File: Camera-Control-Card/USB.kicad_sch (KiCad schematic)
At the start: 15 parts, among them J9 USB_C_Receptacle_USB2.0_16P, U6 TPD2EUSB30, U7 CP2102N-Axx-xQFN20

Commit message: Camera Control Card layout
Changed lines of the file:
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@@
+	)
+	(junction
+		(at 152.4 115.57)
+		(diameter 0)
+		(color 0 0 0 0)
 	)
 	(junction
@@
 	)
 	(junction
+		(at 226.06 50.8)
+		(diameter 0)
+		(color 0 0 0 0)
+	)
+	(junction
 		(at 146.05 115.57)
 		(diameter 0)
@@
 	(wire
 		(pts
+			(xy 152.4 115.57) (xy 153.67 115.57)
+		)
+		(stroke
+			(width 0)
+			(type default)
+		)
+	)
+	(wire
+		(pts
 			(xy 120.65 93.98) (xy 118.11 93.98)
 		)
@@
 		(pts
 			(xy 172.72 82.55) (xy 186.69 82.55)
+		)
+		(stroke
+			(width 0)
+			(type default)
+		)
+	)
+	(wire
+		(pts
+			(xy 226.06 50.8) (xy 227.33 50.8)
 		)
 		(stroke
@@
 		)
 	)
+	(hierarchical_label "+3V3"
+		(shape passive)
+		(at 227.33 50.8 0)
+		(effects
+			(font
+				(size 1.27 1.27)
+			)
+			(justify left)
+		)
+	)
+	(hierarchical_label "GND"
+		(shape passive)
+		(at 153.67 115.57 0)
+		(effects
+			(font
+				(size 1.27 1.27)
+			)
+			(justify left)
+		)
+	)

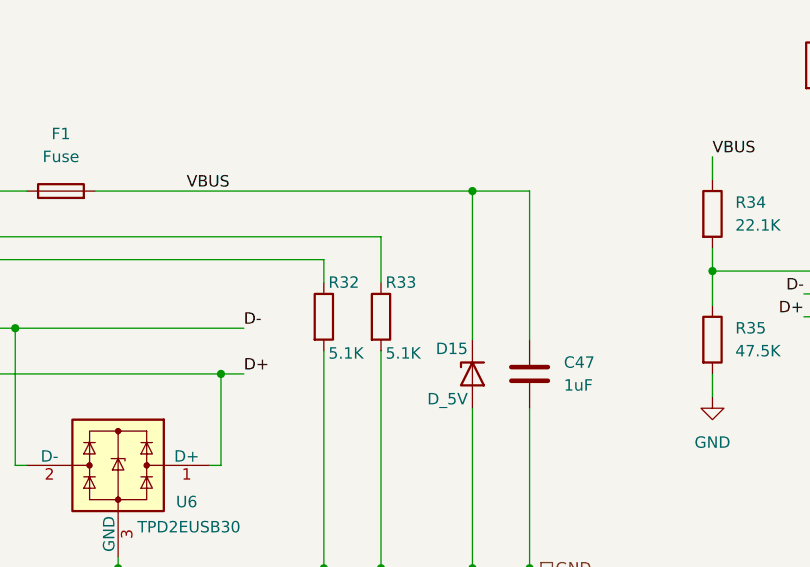
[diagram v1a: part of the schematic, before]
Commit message: Layout completed for camera control card
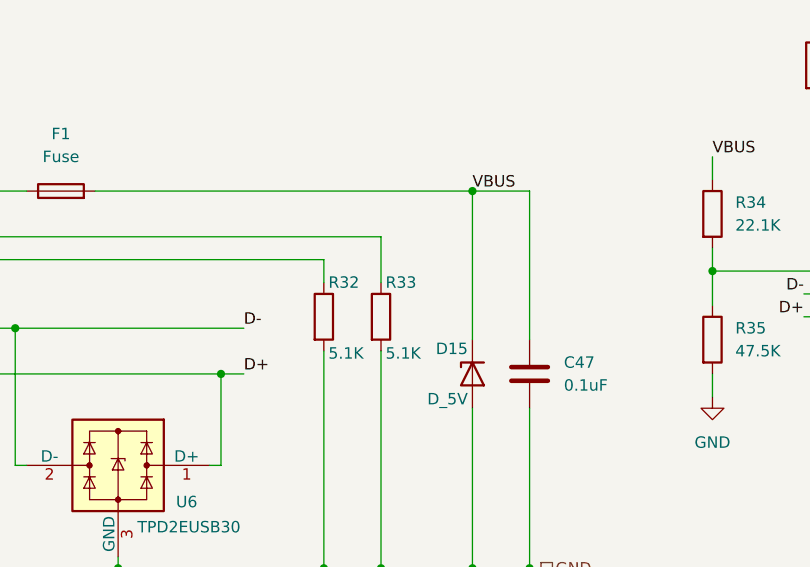
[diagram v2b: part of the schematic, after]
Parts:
- C47: value 1uF -> 0.1uF
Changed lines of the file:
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@@
 	)
 	(label "VBUS"
-		(at 114.3 73.66 0)
+		(at 146.05 73.66 0)
 		(effects
 			(font
@@
 			)
 		)
-		(property "Value" "1uF"
+		(property "Value" "0.1uF"
 			(at 156.21 95.2499 0)
 			(effects
